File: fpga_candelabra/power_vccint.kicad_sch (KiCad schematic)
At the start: 103 parts, among them U2 TPS53667, U3 CSD95491Q5MC, U4 CSD95491Q5MC, U5 CSD95491Q5MC, U6 CSD95491Q5MC

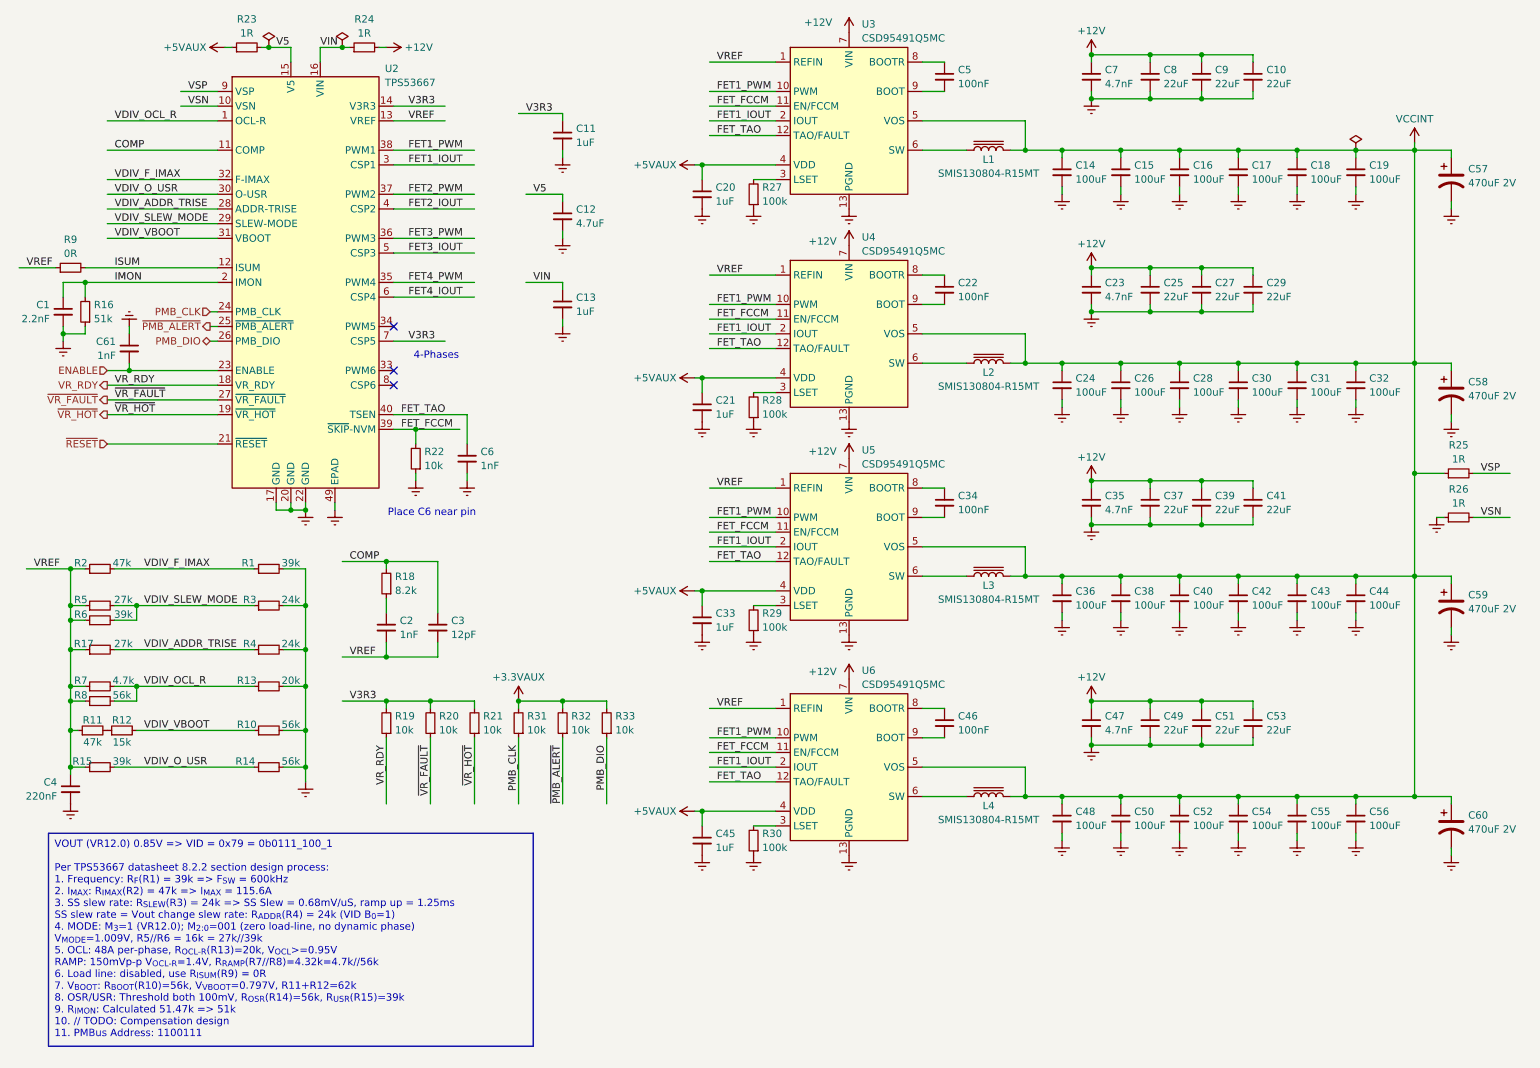
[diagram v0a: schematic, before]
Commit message: fpga_candelabra: finish most FPGA & FMC VADJ power supplies
Signed-off-by: Yichuan Gao <gaoyichuan000@gmail.com>
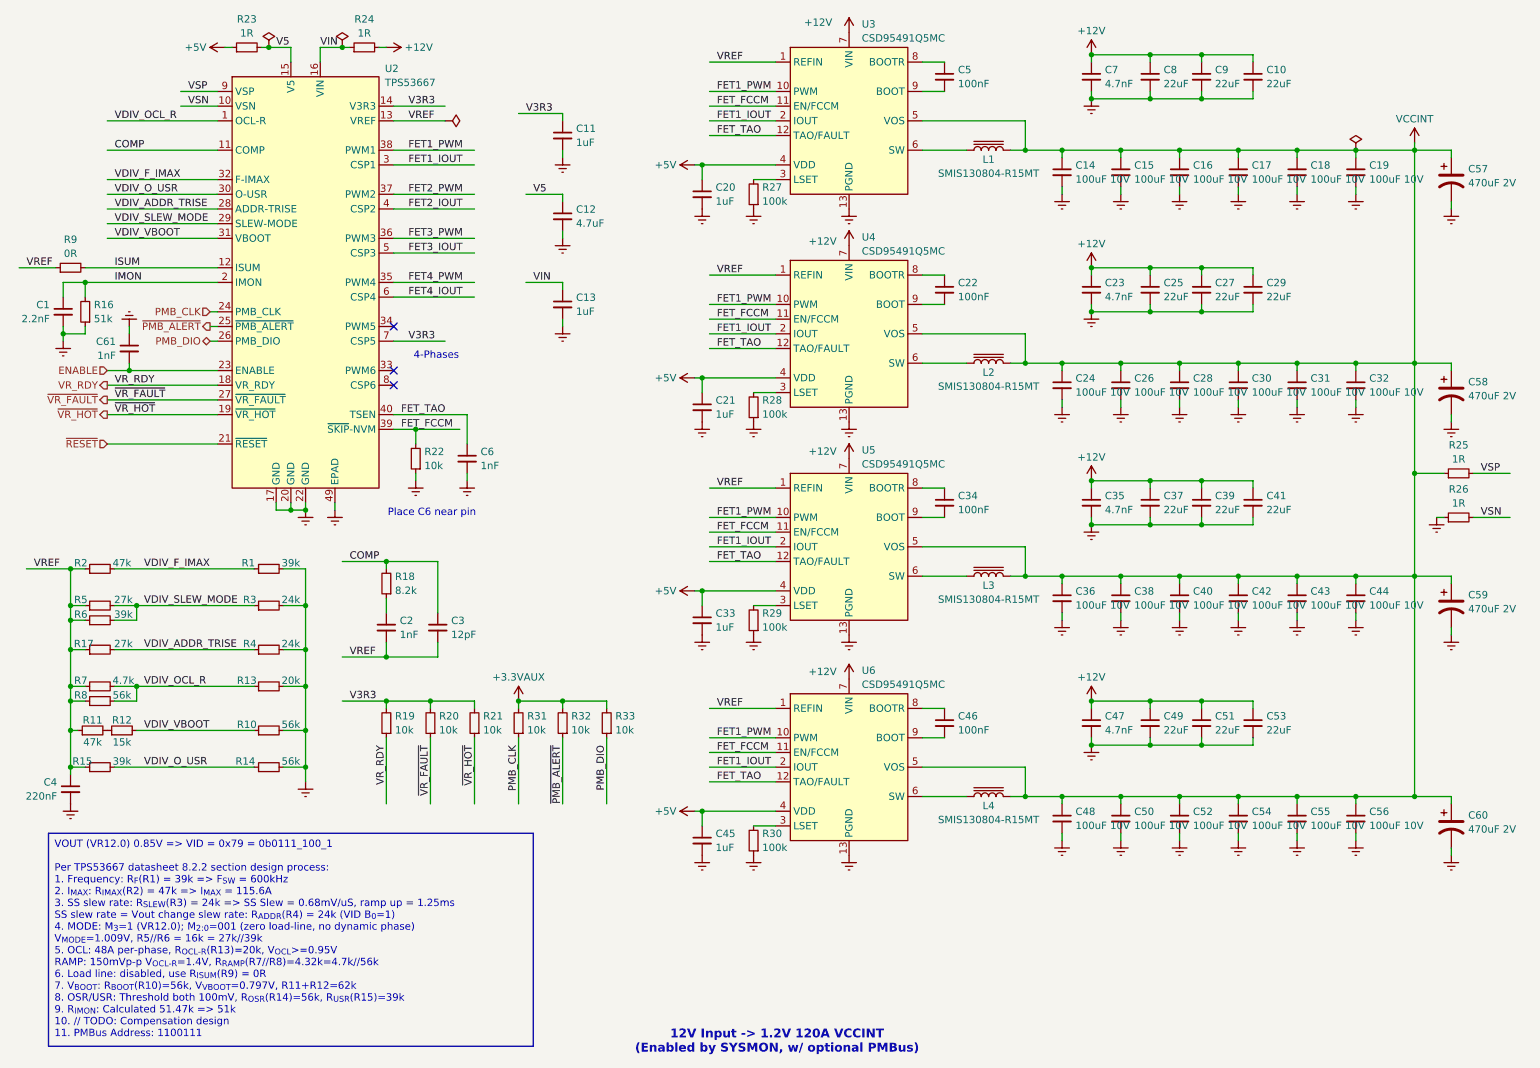
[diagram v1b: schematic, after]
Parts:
- C14, C15, C16, C17, C18, C19, C24, C26, C28, C30, C31, C32, C36, C38, C40, C42, C43, C44, C48, C50, C52, C54, C55, C56: value 100uF -> 100uF 10V
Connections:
- net +5VAUX renamed +5V
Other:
- note added: "12V Input -> 1.2V 120A VCCINT (Enabled by SYSMON, w/ optional PMBus)"
- title: (none) -> Power VCCINT (1.2V 120A 4 Phases)

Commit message: fpga_candelabra: add ddr4 power and sysmon mcu periph, bump library
Signed-off-by: Yichuan Gao <gaoyichuan000@gmail.com>
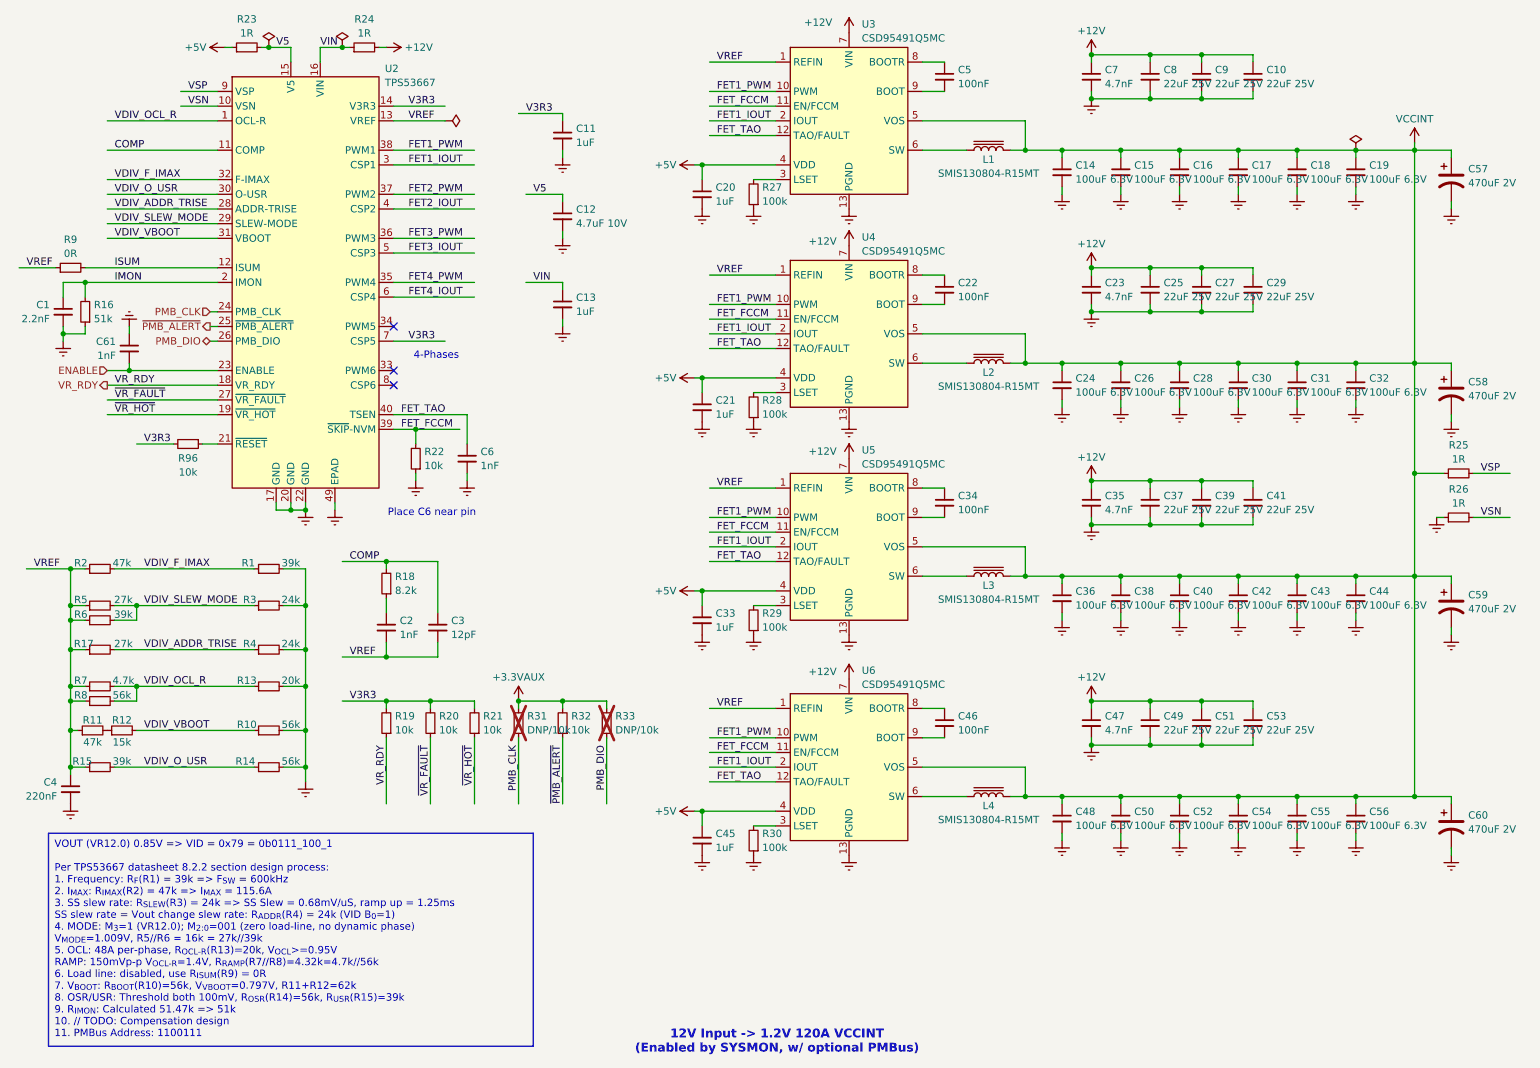
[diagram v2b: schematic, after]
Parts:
- added R96: 10k, Resistor_SMD:R_0402_1005Metric, symbol Device:R_Small
- C10, C25, C27, C29, C37, C39, C41, C49, C51, C53, C8, C9: value 22uF -> 22uF 25V
- C12: value 4.7uF -> 4.7uF 10V
- C14, C15, C16, C17, C18, C19, C24, C26, C28, C30, C31, C32, C36, C38, C40, C42, C43, C44, C48, C50, C52, C54, C55, C56: value 100uF 10V -> 100uF 6.3V
- R31, R33: value 10k -> DNP/10k; now not fitted
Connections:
- net V3R3: now also R96.2
- net ~{RESET}: no longer names the net of U2.21 (~{RESET})
- net ~{RESET}: now also R96.1
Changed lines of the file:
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@@
 	(wire
 		(pts
+			(xy 38.1 88.9) (xy 44.45 88.9)
+		)
+		(stroke
+			(width 0)
+			(type default)
+		)
+	)
+	(wire
+		(pts
 			(xy 86.36 86.36) (xy 86.36 88.9)
 		)
@@
 	(wire
 		(pts
-			(xy 33.02 88.9) (xy 52.07 88.9)
+			(xy 49.53 88.9) (xy 52.07 88.9)
 		)
 		(stroke
@@
 		)
 	)
+	(label "V3R3"
+		(at 39.37 88.9 0)
+		(fields_autoplaced yes)
+		(effects
+			(font
+				(size 1.27 1.27)
+			)
+			(justify left bottom)
+		)
+	)
 	(label "VREF"
 		(at 19.05 58.42 0)
@@
 		)
 	)
-	(hierarchical_label "~{VR_HOT}"
-		(shape output)
-		(at 33.02 83.82 180)
-		(fields_autoplaced yes)
-		(effects
-			(font
-				(size 1.27 1.27)
-			)
-			(justify right)
-		)
-	)
 	(hierarchical_label "PMB_CLK"
 		(shape input)
@@
 		)
 	)
-	(hierarchical_label "~{VR_FAULT}"
-		(shape output)
-		(at 33.02 81.28 180)
-		(fields_autoplaced yes)
-		(effects
-			(font
-				(size 1.27 1.27)
-			)
-			(justify right)
-		)
-	)
 	(hierarchical_label "PMB_DIO"
 		(shape bidirectional)
@@
 		)
 	)
-	(hierarchical_label "~{RESET}"
-		(shape input)
-		(at 33.02 88.9 180)
-		(fields_autoplaced yes)
-		(effects
-			(font
-				(size 1.27 1.27)
-			)
-			(justify right)
-		)
-	)
 	(symbol
 		(lib_id "power:Earth")
@@
 			)
 		)
-		(property "Value" "100uF 10V"
+		(property "Value" "100uF 6.3V"
 			(at 230.9241 79.9584 0)
 			(effects
@@
 		(in_bom yes)
 		(on_board yes)
-		(dnp no)
+		(dnp yes)
 		(fields_autoplaced yes)
 		(property "Reference" "R31"
@@
 			)
 		)
-		(property "Value" "10k"
+		(property "Value" "DNP/10k"
 			(at 105.6386 138.3721 0)
 			(effects
@@
 			)
 		)
-		(property "Value" "100uF 10V"
+		(property "Value" "100uF 6.3V"
 			(at 251.2441 154.8884 0)
 			(effects
@@
 			)
 		)
-		(property "Value" "100uF 10V"
+		(property "Value" "100uF 6.3V"
 			(at 241.0841 116.7884 0)
 			(effects
@@
 			)
 		)
-		(property "Value" "22uF"
+		(property "Value" "22uF 25V"
 			(at 215.6841 100.2784 0)
 			(effects
@@
 			)
 		)
-		(property "Value" "100uF 10V"
+		(property "Value" "100uF 6.3V"
 			(at 251.2441 43.1284 0)
 			(effects
@@
 			)
 		)
-		(property "Value" "100uF 10V"
+		(property "Value" "100uF 6.3V"
 			(at 251.2441 116.7884 0)
 			(effects
@@
 			)
 		)
-		(property "Value" "22uF"
+		(property "Value" "22uF 25V"
 			(at 224.5741 138.3784 0)
 			(effects
@@
 			)
 		)
-		(property "Value" "22uF"
+		(property "Value" "22uF 25V"
 			(at 215.6841 26.6184 0)
 			(effects
@@
 			)
 		)
-		(property "Value" "22uF"
+		(property "Value" "22uF 25V"
 			(at 215.6841 138.3784 0)
 			(effects
@@
 			)
 		)
-		(property "Value" "22uF"
+		(property "Value" "22uF 25V"
 			(at 233.4641 100.2784 0)
 			(effects
@@
 			)
 		)
-		(property "Value" "100uF 10V"
+		(property "Value" "100uF 6.3V"
 			(at 251.2441 79.9584 0)
 			(effects
@@
 			)
 		)
-		(property "Value" "22uF"
+		(property "Value" "22uF 25V"
 			(at 233.4641 26.6184 0)
 			(effects
@@
 			)
 		)
-		(property "Value" "100uF 10V"
+		(property "Value" "100uF 6.3V"
 			(at 220.7641 154.8884 0)
 			(effects
@@
 			)
 		)
-		(property "Value" "100uF 10V"
+		(property "Value" "100uF 6.3V"
 			(at 241.0841 79.9584 0)
 			(effects
@@
 			)
 		)
-		(property "Value" "100uF 10V"
+		(property "Value" "100uF 6.3V"
 			(at 210.6041 116.7884 0)
 			(effects
@@
 			)
 		)
-		(property "Value" "100uF 10V"
+		(property "Value" "100uF 6.3V"
 			(at 210.6041 154.8884 0)
 			(effects
@@
 			)
 		)
-		(property "Value" "100uF 10V"
+		(property "Value" "100uF 6.3V"
 			(at 241.0841 154.8884 0)
 			(effects
@@
 			)
 		)
-		(property "Value" "22uF"
+		(property "Value" "22uF 25V"
 			(at 224.5741 63.4484 0)
 			(effects
@@
 			)
 		)
-		(property "Value" "100uF 10V"
+		(property "Value" "100uF 6.3V"
 			(at 230.9241 43.1284 0)
 			(effects
@@
 			)
 		)
-		(property "Value" "100uF 10V"
+		(property "Value" "100uF 6.3V"
 			(at 200.4441 154.8884 0)
 			(effects
@@
 			)
 		)
-		(property "Value" "22uF"
+		(property "Value" "22uF 25V"
 			(at 233.4641 138.3784 0)
 			(effects
@@
 	)
 	(symbol
+		(lib_id "Device:R_Small")
+		(at 46.99 88.9 270)
+		(unit 1)
+		(exclude_from_sim no)
+		(in_bom yes)
+		(on_board yes)
+		(dnp no)
+		(fields_autoplaced yes)
+		(property "Reference" "R96"
+			(at 46.99 91.3567 90)
+			(effects
+				(font
+					(size 1.27 1.27)
+				)
+			)
+		)
+		(property "Value" "10k"
+			(at 46.99 93.781 90)
+			(effects
+				(font
+					(size 1.27 1.27)
+				)
+			)
+		)
+		(property "Footprint" "Resistor_SMD:R_0402_1005Metric"
+			(at 46.99 88.9 0)
+			(effects
+				(font
+					(size 1.27 1.27)
+				)
+				(hide yes)
+			)
+		)
+		(property "Datasheet" "~"
+			(at 46.99 88.9 0)
+			(effects
+				(font
+					(size 1.27 1.27)
+				)
+				(hide yes)
+			)
+		)
+		(property "Description" "Resistor, small symbol"
+			(at 46.99 88.9 0)
+			(effects
+				(font
+					(size 1.27 1.27)
+				)
+				(hide yes)
+			)
+		)
+		(pin "2"
+		)
+		(pin "1"
+		)
+		(instances
+			(project "fpga_candelabra"
+				(path "/01ed9e92-4e50-4b41-90dc-10444aaec5f7/beaa4e74-1d18-44b4-b7c5-122d2a26ede8"
+					(reference "R96")
+					(unit 1)
+				)
+			)
+		)
+	)
+	(symbol
 		(lib_id "power:Earth")
 		(at 238.76 82.55 0)
@@
 			)
 		)
-		(property "Value" "22uF"
+		(property "Value" "22uF 25V"
 			(at 215.6841 63.4484 0)
 			(effects
@@
 			)
 		)
-		(property "Value" "100uF 10V"
+		(property "Value" "100uF 6.3V"
 			(at 220.7641 79.9584 0)
 			(effects
@@
 			)
 		)
-		(property "Value" "100uF 10V"
+		(property "Value" "100uF 6.3V"
 			(at 241.0841 43.1284 0)
 			(effects
@@
 			)
 		)
-		(property "Value" "100uF 10V"
+		(property "Value" "100uF 6.3V"
 			(at 220.7641 116.7884 0)
 			(effects
@@
 			)
 		)
-		(property "Value" "22uF"
+		(property "Value" "22uF 25V"
 			(at 224.5741 100.2784 0)
 			(effects
@@
 			)
 		)
-		(property "Value" "4.7uF"
+		(property "Value" "4.7uF 10V"
 			(at 114.0841 50.7484 0)
 			(effects
@@
 			)
 		)
-		(property "Value" "100uF 10V"
+		(property "Value" "100uF 6.3V"
 			(at 220.7641 43.1284 0)
 			(effects
@@
 			)
 		)
-		(property "Value" "100uF 10V"
+		(property "Value" "100uF 6.3V"
 			(at 200.4441 43.1284 0)
 			(effects
@@
 			)
 		)
-		(property "Value" "22uF"
+		(property "Value" "22uF 25V"
 			(at 224.5741 26.6184 0)
 			(effects
@@
 			)
 		)
-		(property "Value" "100uF 10V"
+		(property "Value" "100uF 6.3V"
 			(at 210.6041 79.9584 0)
 			(effects
@@
 			)
 		)
-		(property "Value" "100uF 10V"
+		(property "Value" "100uF 6.3V"
 			(at 200.4441 79.9584 0)
 			(effects
@@
 			)
 		)
-		(property "Value" "100uF 10V"
+		(property "Value" "100uF 6.3V"
 			(at 230.9241 154.8884 0)
 			(effects
@@
 		(in_bom yes)
 		(on_board yes)
-		(dnp no)
+		(dnp yes)
 		(fields_autoplaced yes)
 		(property "Reference" "R33"
@@
 			)
 		)
-		(property "Value" "10k"
+		(property "Value" "DNP/10k"
 			(at 120.8786 138.3721 0)
 			(effects
@@
 			)
 		)
-		(property "Value" "100uF 10V"
+		(property "Value" "100uF 6.3V"
 			(at 210.6041 43.1284 0)
 			(effects
@@
 			)
 		)
-		(property "Value" "100uF 10V"
+		(property "Value" "100uF 6.3V"
 			(at 230.9241 116.7884 0)
 			(effects
@@
 			)
 		)
-		(property "Value" "100uF 10V"
+		(property "Value" "100uF 6.3V"
 			(at 200.4441 116.7884 0)
 			(effects
@@
 			)
 		)
-		(property "Value" "22uF"
+		(property "Value" "22uF 25V"
 			(at 233.4641 63.4484 0)
 			(effects

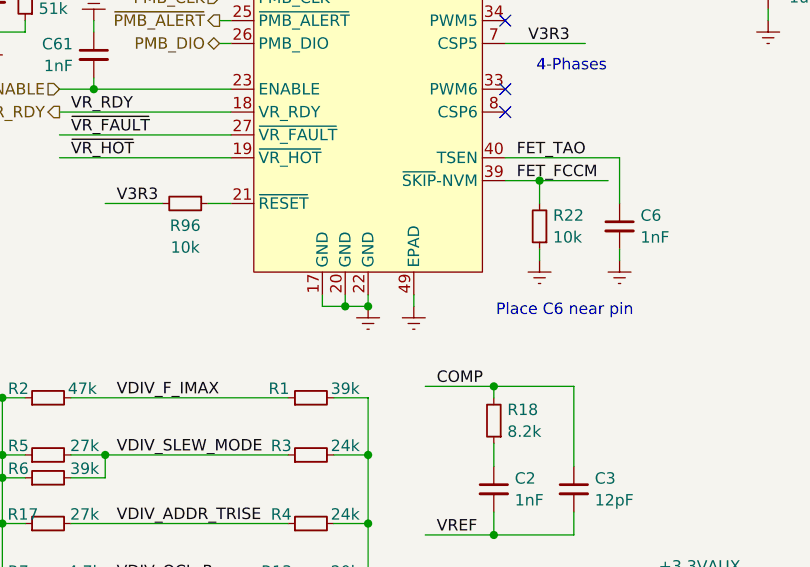
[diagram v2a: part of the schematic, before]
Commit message: fpga_candelabra: add clock pll, refactor fmc power
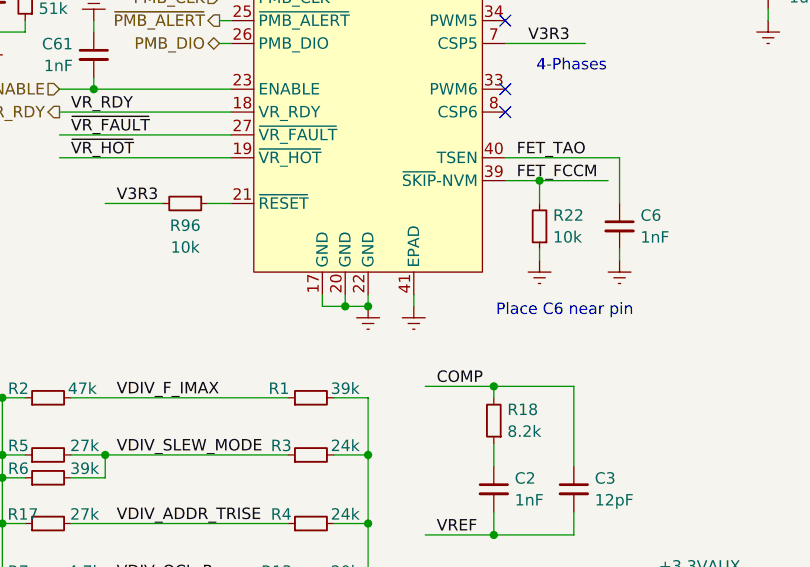
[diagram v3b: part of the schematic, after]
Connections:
- net Earth: now also U2.41 (EPAD); no longer U2.49 (EPAD)
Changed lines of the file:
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@@
 		(pin "12"
 		)
-		(pin "49"
+		(pin "41"
 		)
 		(pin "11"
